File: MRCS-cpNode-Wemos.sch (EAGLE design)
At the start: 28 parts, among them CON5 3.5mm, J1 2.1mm, Q1 2n7002, Q2 2n7002, Q3 2n7002, Q4 2n7002, Q5 2n7002

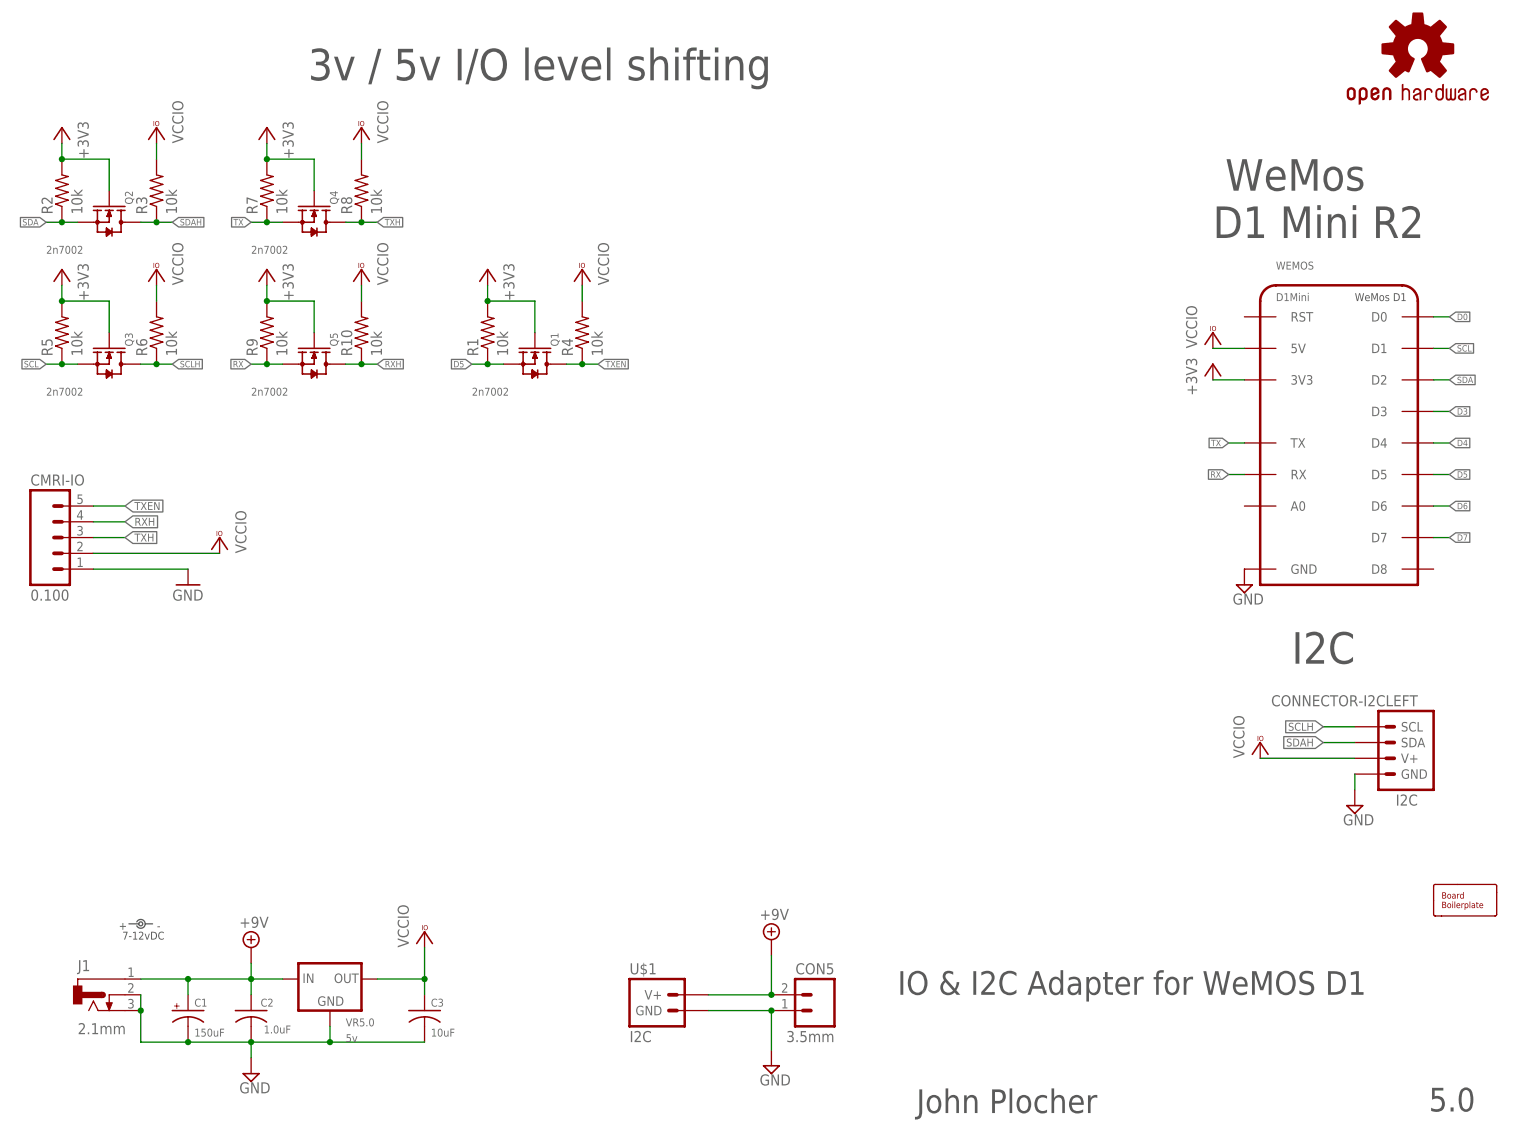
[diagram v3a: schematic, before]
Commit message: normalized values
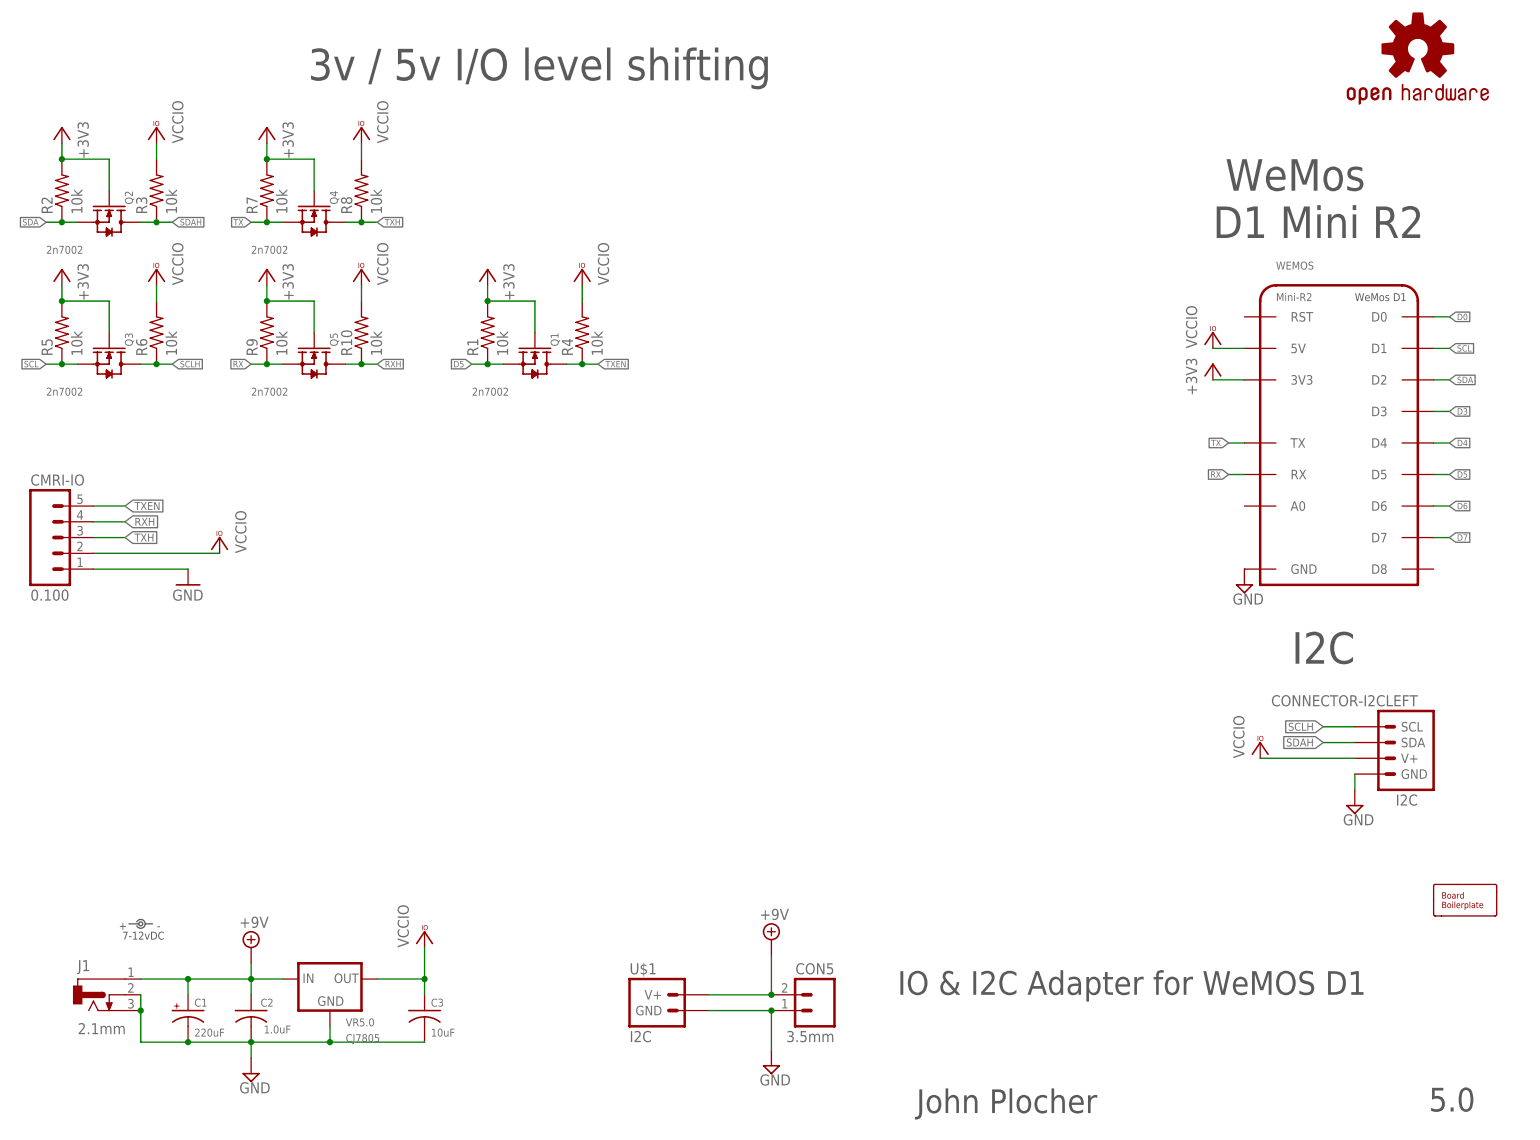
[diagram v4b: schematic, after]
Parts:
- BOARD: value BOARD80X150 -> BOARD
- C1: value 150uF -> 220uF
- C2, C3: device SPCoast:CAP0805 -> SPCoast:CAP0603
- OSHW1: value OSHW-LOGOL -> OSHW
- R10, R2, R3, R4, R5, R6, R7, R8, R9: device SPCoast:R0805-RES -> SPCoast:R0603-RES
- VR5.0: value 5v -> CJ7805
- WEMOS: value D1Mini -> Mini-R2
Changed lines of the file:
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@@
 <parts>
 <part name="FRAME1" library="MCP" deviceset="FRAME-LETTER" device=""/>
-<part name="OSHW1" library="SparkFun" deviceset="OSHW-LOGO" device="L" value="OSHW-LOGOL"/>
+<part name="OSHW1" library="SparkFun" deviceset="OSHW-LOGO" device="L" value="OSHW"/>
 <part name="SUPPLY2" library="supply2" deviceset="+9V" device=""/>
 <part name="V12" library="supply2" deviceset="GND" device=""/>
@@
 <part name="LABEL1" library="SPCoast" deviceset="DOC-POWER_LABEL" device="" value="7-12vDC"/>
 <part name="VCC12" library="supply1" deviceset="VCCIO" device=""/>
-<part name="BOARD" library="SPCoast" deviceset="BOARD" device="69X80" value="BOARD80X150"/>
-<part name="C3" library="SPCoast" deviceset="CAP*" device="0805" value="10uF"/>
-<part name="C2" library="SPCoast" deviceset="CAP*" device="0805" value="1.0uF"/>
-<part name="VR5.0" library="SPCoast" deviceset="VREG-?-*" device="DPAK" technology="5" value="5v"/>
-<part name="WEMOS" library="SPCoast" deviceset="WEMOS-D1" device="V1" value="D1Mini"/>
+<part name="BOARD" library="SPCoast" deviceset="BOARD" device="69X80" value="BOARD"/>
+<part name="C3" library="SPCoast" deviceset="CAP*" device="0603" value="10uF"/>
+<part name="C2" library="SPCoast" deviceset="CAP*" device="0603" value="1.0uF"/>
+<part name="VR5.0" library="SPCoast" deviceset="VREG-?-*" device="DPAK" technology="5" value="CJ7805"/>
+<part name="WEMOS" library="SPCoast" deviceset="WEMOS-D1" device="V1" value="Mini-R2"/>
 <part name="V7" library="supply2" deviceset="GND" device=""/>
 <part name="3V18" library="supply1" deviceset="+3V3" device=""/>
 <part name="VCC24" library="supply1" deviceset="VCCIO" device=""/>
 <part name="VCC8" library="supply1" deviceset="VCCIO" device=""/>
-<part name="C1" library="SPCoast" deviceset="CAP-POL*" device="0810" value="150uF"/>
+<part name="C1" library="SPCoast" deviceset="CAP-POL*" device="0810" value="220uF"/>
 <part name="Q2" library="SPCoast" deviceset="MOSFET-N-*-?" device="SOT23" technology="BSS138" value="2n7002"/>
-<part name="R2" library="SPCoast" deviceset="R*" device="0805-RES" value="10k"/>
-<part name="R3" library="SPCoast" deviceset="R*" device="0805-RES" value="10k"/>
+<part name="R2" library="SPCoast" deviceset="R*" device="0603-RES" value="10k"/>
+<part name="R3" library="SPCoast" deviceset="R*" device="0603-RES" value="10k"/>
 <part name="3V3" library="supply1" deviceset="+3V3" device=""/>
 <part name="VCC5" library="supply1" deviceset="VCCIO" device=""/>
 <part name="Q3" library="SPCoast" deviceset="MOSFET-N-*-?" device="SOT23" technology="BSS138" value="2n7002"/>
-<part name="R5" library="SPCoast" deviceset="R*" device="0805-RES" value="10k"/>
-<part name="R6" library="SPCoast" deviceset="R*" device="0805-RES" value="10k"/>
+<part name="R5" library="SPCoast" deviceset="R*" device="0603-RES" value="10k"/>
+<part name="R6" library="SPCoast" deviceset="R*" device="0603-RES" value="10k"/>
 <part name="3V5" library="supply1" deviceset="+3V3" device=""/>
 <part name="VCC7" library="supply1" deviceset="VCCIO" device=""/>
 <part name="Q4" library="SPCoast" deviceset="MOSFET-N-*-?" device="SOT23" technology="BSS138" value="2n7002"/>
-<part name="R7" library="SPCoast" deviceset="R*" device="0805-RES" value="10k"/>
-<part name="R8" library="SPCoast" deviceset="R*" device="0805-RES" value="10k"/>
+<part name="R7" library="SPCoast" deviceset="R*" device="0603-RES" value="10k"/>
+<part name="R8" library="SPCoast" deviceset="R*" device="0603-RES" value="10k"/>
 <part name="3V1" library="supply1" deviceset="+3V3" device=""/>
 <part name="VCC1" library="supply1" deviceset="VCCIO" device=""/>
 <part name="Q5" library="SPCoast" deviceset="MOSFET-N-*-?" device="SOT23" technology="BSS138" value="2n7002"/>
-<part name="R9" library="SPCoast" deviceset="R*" device="0805-RES" value="10k"/>
-<part name="R10" library="SPCoast" deviceset="R*" device="0805-RES" value="10k"/>
+<part name="R9" library="SPCoast" deviceset="R*" device="0603-RES" value="10k"/>
+<part name="R10" library="SPCoast" deviceset="R*" device="0603-RES" value="10k"/>
 <part name="3V6" library="supply1" deviceset="+3V3" device=""/>
 <part name="VCC9" library="supply1" deviceset="VCCIO" device=""/>
@@
 <part name="Q1" library="SPCoast" deviceset="MOSFET-N-*-?" device="SOT23" technology="BSS138" value="2n7002"/>
 <part name="R1" library="SPCoast" deviceset="R*" device="0805-RES" value="10k"/>
-<part name="R4" library="SPCoast" deviceset="R*" device="0805-RES" value="10k"/>
+<part name="R4" library="SPCoast" deviceset="R*" device="0603-RES" value="10k"/>
 <part name="3V2" library="supply1" deviceset="+3V3" device=""/>
 <part name="VCC2" library="supply1" deviceset="VCCIO" device=""/>
@@
 <instance part="VCC9" gate="G$1" x="63.5" y="142.24" rot="MR0"/>
 <instance part="CON5" gate="J" x="134.62" y="22.86" rot="MR0"/>
-<instance part="CMRI-IO" gate="G$1" x="12.7" y="99.06"/>
+<instance part="CMRI-IO" gate="CON1" x="12.7" y="99.06"/>
 <instance part="GND1" gate="1" x="35.56" y="91.44"/>
 <instance part="Q1" gate="Q" x="91.44" y="127" smashed="yes" rot="R270">
@@
 </segment>
 <segment>
-<pinref part="CMRI-IO" gate="G$1" pin="1"/>
+<pinref part="CMRI-IO" gate="CON1" pin="1"/>
 <wire x1="20.32" y1="93.98" x2="35.56" y2="93.98" width="0.1524" layer="91"/>
 <pinref part="GND1" gate="1" pin="GND"/>
@@
 </segment>
 <segment>
-<pinref part="CMRI-IO" gate="G$1" pin="2"/>
+<pinref part="CMRI-IO" gate="CON1" pin="2"/>
 <wire x1="20.32" y1="96.52" x2="40.64" y2="96.52" width="0.1524" layer="91"/>
 <pinref part="VCC3" gate="G$1" pin="VCCIO"/>
@@
 </segment>
 <segment>
-<pinref part="CMRI-IO" gate="G$1" pin="4"/>
+<pinref part="CMRI-IO" gate="CON1" pin="4"/>
 <wire x1="20.32" y1="101.6" x2="25.4" y2="101.6" width="0.1524" layer="91"/>
 <label x="25.4" y="101.6" size="1.27" layer="95" xref="yes"/>
@@
 </segment>
 <segment>
-<pinref part="CMRI-IO" gate="G$1" pin="3"/>
+<pinref part="CMRI-IO" gate="CON1" pin="3"/>
 <wire x1="20.32" y1="99.06" x2="25.4" y2="99.06" width="0.1524" layer="91"/>
 <label x="25.4" y="99.06" size="1.27" layer="95" xref="yes"/>
@@
 <net name="TXEN" class="0">
 <segment>
-<pinref part="CMRI-IO" gate="G$1" pin="5"/>
+<pinref part="CMRI-IO" gate="CON1" pin="5"/>
 <wire x1="20.32" y1="104.14" x2="25.4" y2="104.14" width="0.1524" layer="91"/>
 <label x="25.4" y="104.14" size="1.27" layer="95" xref="yes"/>
